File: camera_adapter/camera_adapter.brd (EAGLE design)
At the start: 51 x 24 mm, 1 part

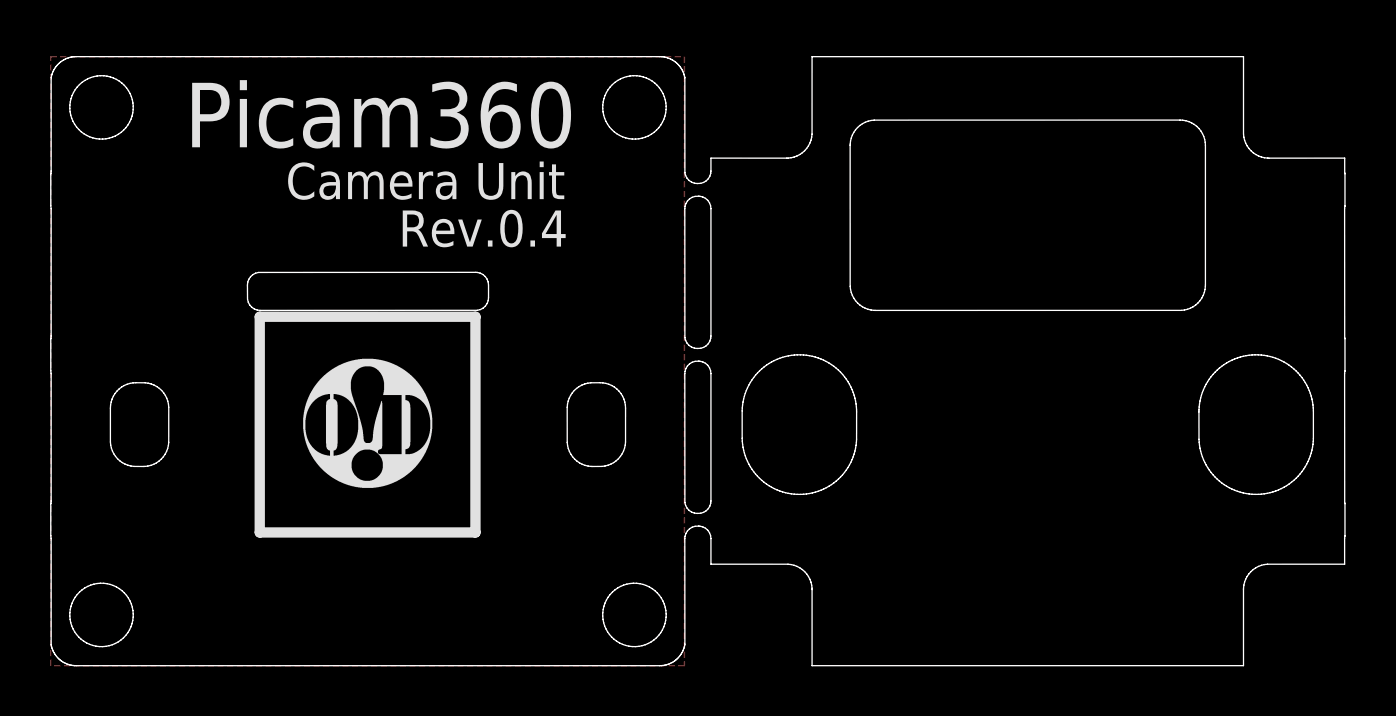
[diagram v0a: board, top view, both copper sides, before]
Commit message: camera_unit, camera_adapter
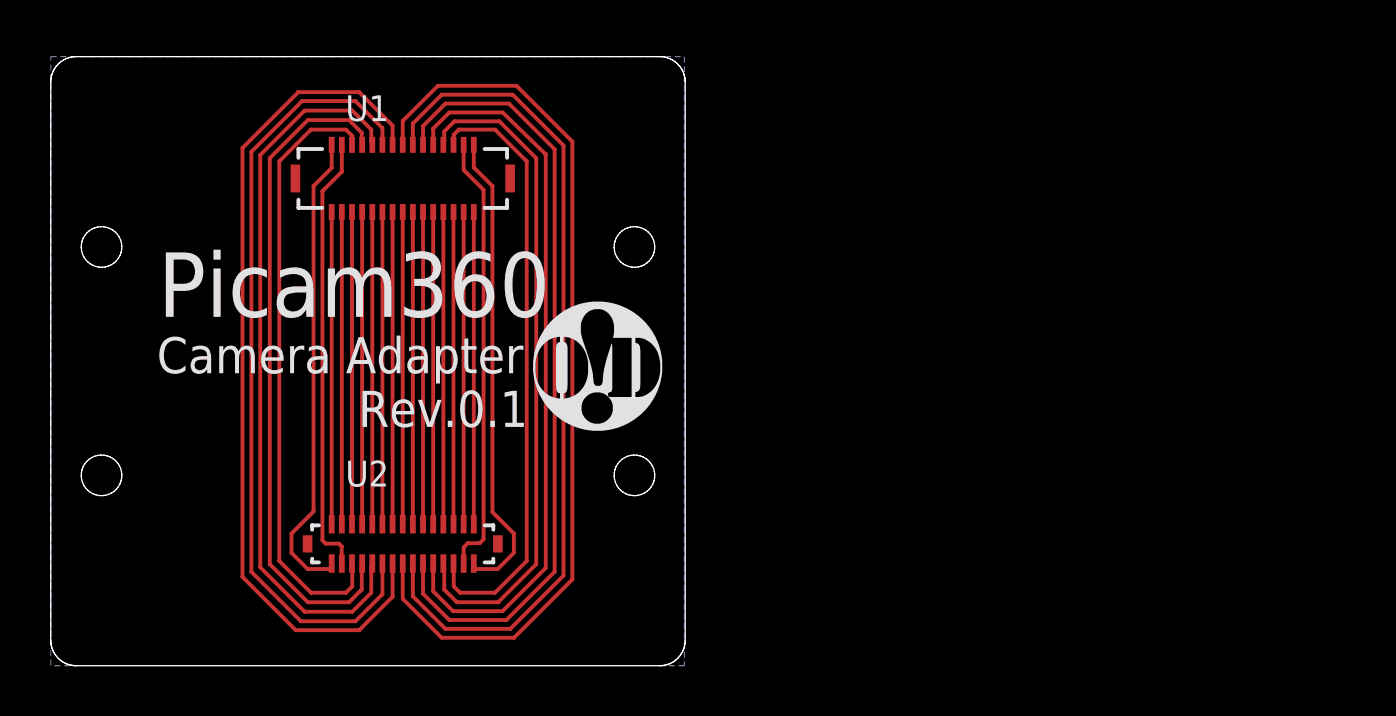
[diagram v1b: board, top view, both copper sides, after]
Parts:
- added U1: DF37NC-30DS-0.4V, openblw:DF37**-30DS-0.4V
- added U2: DF37C-30DP-0.4V, openblw:DF37**-30DP-0.4V
- moved LOGO1 9.34 mm to (21.6, 11.8)
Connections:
- new net N$1: U1.2, U2.2
- new net N$10: U1.20, U2.20
- new net N$11: U1.22, U2.22
- new net N$12: U1.24, U2.24
- new net N$13: U1.26, U2.26
- new net N$14: U1.28, U2.28
- new net N$15: U1.30, U2.30
- new net N$16: U1.1, U2.1
- new net N$17: U1.3, U2.3
- new net N$18: U1.5, U2.5
- new net N$19: U1.7, U2.7
- new net N$2: U1.4, U2.4
- new net N$20: U1.9, U2.9
- new net N$21: U1.11, U2.11
- new net N$22: U1.13, U2.13
- new net N$23: U1.15, U2.15
- new net N$24: U1.29, U2.29
- new net N$25: U1.27, U2.27
- new net N$26: U1.25, U2.25
- new net N$27: U1.23, U2.23
- new net N$28: U1.21, U2.21
- new net N$29: U1.19, U2.19
- new net N$3: U1.6, U2.6
- new net N$30: U1.17, U2.17
- new net N$4: U1.8, U2.8
- new net N$5: U1.10, U2.10
- new net N$6: U1.12, U2.12
- new net N$7: U1.14, U2.14
- new net N$8: U1.16, U2.16
- new net N$9: U1.18, U2.18
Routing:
- net N$8: track 0.00 -> 36.0 mm
- net N$9: track 0.00 -> 33.7 mm
- net N$7: track 0.00 -> 33.7 mm
- net N$6: track 0.00 -> 31.3 mm
- net N$10: track 0.00 -> 31.3 mm
- net N$5: track 0.00 -> 28.9 mm
- net N$11: track 0.00 -> 28.8 mm
- net N$12: track 0.00 -> 26.4 mm
- net N$4: track 0.00 -> 26.4 mm
- net N$3: track 0.00 -> 24.0 mm
- net N$13: track 0.00 -> 24.0 mm
- net N$15: track 0.00 -> 18.7 mm
- net N$1: track 0.00 -> 18.7 mm
- net N$2: track 0.00 -> 17.5 mm
- net N$14: track 0.00 -> 17.4 mm
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- added copper zone on layer 16, net N$31
- removed copper zone on layer 1, net N$31
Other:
- board size 51 x 24 mm -> 25 x 24 mm
- board text added: "Camera Adapter"
- board text added: "Rev.0.1"
- board text removed: "Camera Unit"
- board text removed: "Rev.0.4"

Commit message: interface board 0.7 rpcm board 0.10
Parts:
- moved LOGO1 14.2 mm to (7.78, 8.22)
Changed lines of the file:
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@@
 <attribute name="VALUE" x="11.5332" y="1.498" size="1.016" layer="27" ratio="10" rot="SR0" display="off"/>
 </element>
-<element name="LOGO1" library="openblw" package="OHMYDIGIFAB_LOGO" value="" x="21.562" y="11.753" smashed="yes"/>
+<element name="LOGO1" library="openblw" package="OHMYDIGIFAB_LOGO" value="" x="7.783" y="8.218" smashed="yes"/>
 </elements>
 <signals>
